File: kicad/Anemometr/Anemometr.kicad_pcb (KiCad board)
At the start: 2 copper layers, 44.9 x 45.2 mm, 161 parts, among them J10 +Z3, J11 -Z3, J12 +Z4, J13 -Z4, J14 SWD, J15 SWC, J18 1 TxD+, J19 2 TxD-, J2 Conn_01x01_Female, J20 3 RxD+, J21 4-5, J23 6 RxD-, J24 7-8, J3 RST, J36 TMP117, J37 TMP117, J38 TMP117, J39 TMP117, J4 TxD, J5 RxD, J6 +Z1, J7 -Z1, J8 +Z2, J9 -Z2, Q1 5N10, U1 TS5A3166DBVR, U10 MCP1700-3002E, U2 LMV7239, U3 TS5A3166DBVR, U4 TS5A3166DBVR, U5 STM32F103C8Tx, U6 TS5A3166DBVR, U7 LM2734Y, U8 MCP1700-5002E, U9 MCP1700-3002E, Y1 8MHz, Y2 25MHz

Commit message: изменено:      kicad/Anemometr/Anemometr-cache.lib 	изменено:      kicad/Anemometr/Anemometr.kicad_pcb 	изменено:      kicad/Anemometr/Anemometr.kicad_pcb-bak 	изменено:      kicad/Anemometr/Anemometr.sch 	изменено:      kicad/Anemometr/Anemometr.sch-bak
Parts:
- removed L6: 47uH, Inductor_SMD:L_0805_2012Metric
- C29: value 10uF -> 10nF
- C30: value 10uF -> 4.7uF
- C50: moved to B.Cu
- L4: value 47uH -> 2.2uH
- U10: value MCP1700-3002E -> AP1117-33; footprint Package_TO_SOT_SMD:SOT-23 -> Package_TO_SOT_SMD:SOT-223-3_TabPin2; moved to B.Cu
- moved C50 23.2 mm to (59.3, 88.5), turned to 0 degrees
- moved U10 13.7 mm to (57.5, 83.9), turned to 180 degrees
- moved D18 8.98 mm to (51.6, 102.9)
- moved C49 8.80 mm to (60.1, 94.5)
- moved D14 7.72 mm to (58.0, 100.7), turned to 180 degrees
- moved R43 6.84 mm to (55.0, 102.8), turned to 0 degrees
- moved L5 6.56 mm to (58.4, 102.9)
- moved R30 5.32 mm to (35.6, 87.6)
- moved R29 5.29 mm to (34.2, 87.6)
- moved D11 3.86 mm to (30.9, 85.0)
- moved R16 3.75 mm to (41.6, 86.8), turned to 0 degrees
- moved D2 3.44 mm to (26.9, 80.5), turned to 90 degrees
- moved C33 2.27 mm to (41.7, 91.4), turned to 180 degrees
- moved C47 2.11 mm to (34.7, 85.5), turned to 0 degrees
- moved C16 1.90 mm to (25.1, 81.2)
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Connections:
- C50 pad 2: Net-(C50-Pad2) -> Net-(C49-Pad1)
- U10 pad 3: Net-(C50-Pad2) -> Net-(C49-Pad1)
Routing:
- net +3.3VDAC: track 29.8 -> 40.9 mm, vias 2 -> 3
- net Net-(C49-Pad1): track 10.0 -> 20.9 mm
- net Net-(C50-Pad2): track 9.93 -> 0.00 mm
- net Net-(C22-Pad2): track 67.7 -> 63.1 mm
- net Net-(C16-Pad2): track 7.19 -> 11.8 mm
- net Net-(C45-Pad2): track 36.7 -> 32.8 mm
- net Net-(C17-Pad2): track 21.7 -> 19.0 mm
- net GND: track 236.5 -> 233.9 mm, vias 16 -> 17
- net Net-(D11-Pad2): track 14.9 -> 17.4 mm
- net Net-(C33-Pad2): track 4.31 -> 1.78 mm
- net Net-(C52-Pad1): track 7.34 -> 4.98 mm
- net Net-(D14-Pad2): track 8.81 -> 7.24 mm
- net Net-(C33-Pad1): track 4.99 -> 3.46 mm
- net +3.3VA: track 34.1 -> 33.3 mm, vias 5 -> 3
- net Net-(C34-Pad1): track 5.38 -> 6.08 mm
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
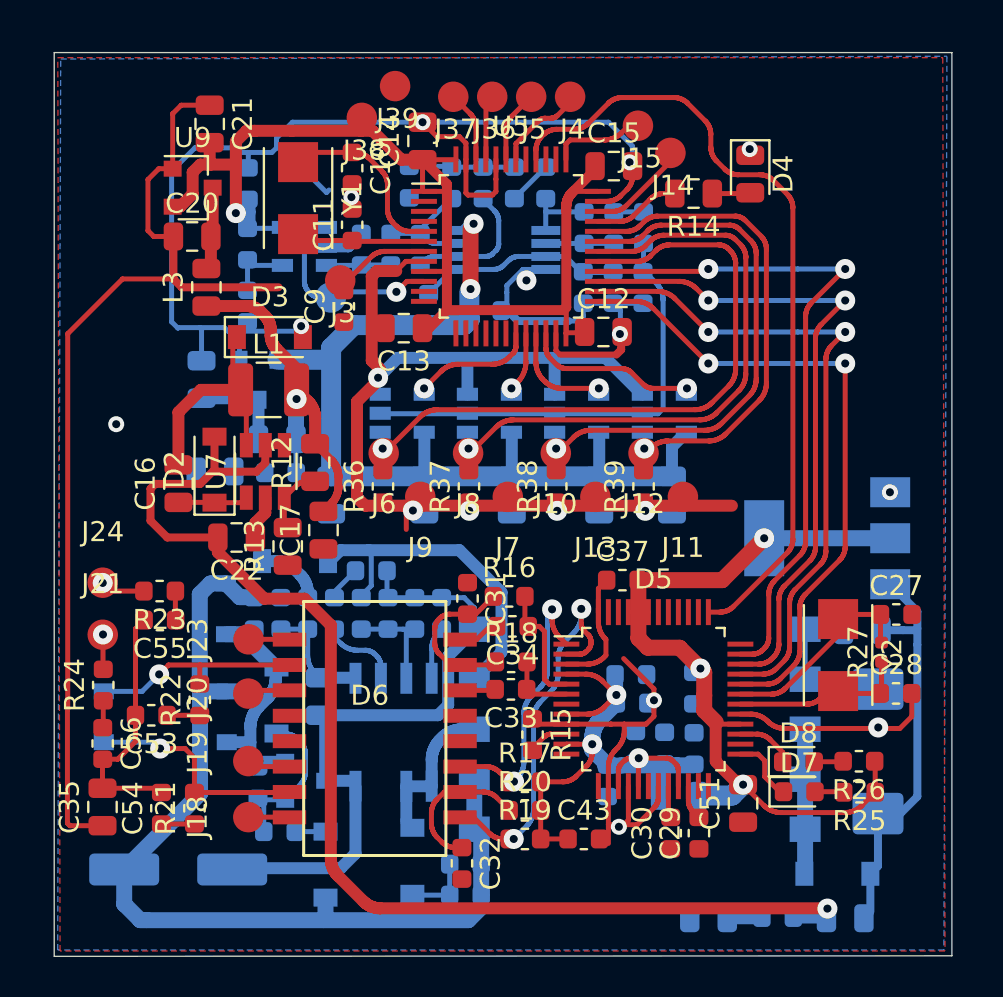
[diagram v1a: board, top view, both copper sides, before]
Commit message: изменено:      kicad/Anemometr/Anemometr.kicad_pcb 	изменено:      kicad/Anemometr/Anemometr.kicad_pcb-bak 	изменено:      kicad/Anemometr/Anemometr.sch 	изменено:      kicad/Anemometr/Anemometr.sch-bak
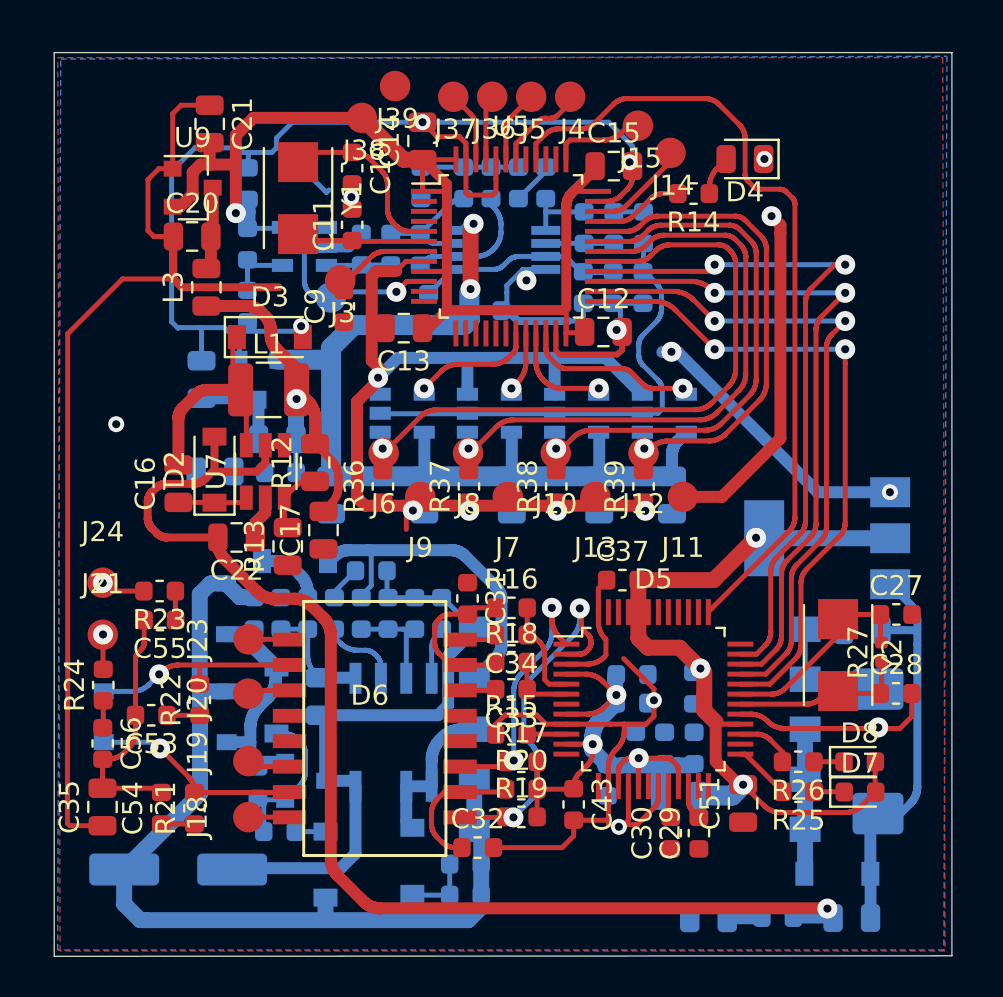
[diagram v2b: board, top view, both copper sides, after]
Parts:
- L1: value 10uH -> 22uH
- R14: footprint Resistor_SMD:R_0805_2012Metric -> Resistor_SMD:R_0603_1608Metric
- moved D8 3.06 mm to (59.1, 95.1)
- moved R25 3.05 mm to (56.1, 96.6)
- moved R26 3.04 mm to (56.1, 95.1)
- moved D7 3.04 mm to (59.2, 96.6)
- moved C43 1.80 mm to (44.8, 97.2), turned to 270 degrees
- moved R19 1.12 mm to (42.2, 97.8)
- moved C32 1.11 mm to (40.0, 99.4), turned to 0 degrees
- moved R20 1.08 mm to (42.2, 96.4)
- moved R15 1.05 mm to (41.7, 93.7), turned to 0 degrees
- moved R17 1.02 mm to (42.2, 95.1)
- moved D4 0.80 mm to (53.4, 64.9), turned to 180 degrees
- moved C3 0.60 mm to (39.3, 66.1)
- moved R9 0.59 mm to (37.2, 66.1)
- moved R16 0.58 mm to (41.7, 87.4)
- moved C34 0.43 mm to (41.7, 88.7)
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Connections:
- D7 pad 1: Net-(D5-Pad25) -> Net-(D7-Pad1)
- D7 pad 2: Net-(D7-Pad2) -> +3.3VDAC
- D8 pad 1: Net-(D5-Pad27) -> Net-(D8-Pad1)
- D8 pad 2: Net-(D8-Pad2) -> +3.3VDAC
- R25 pad 1: +3.3VDAC -> Net-(D7-Pad1)
- R25 pad 2: Net-(D7-Pad2) -> Net-(D5-Pad25)
- R26 pad 1: +3.3VDAC -> Net-(D8-Pad1)
- R26 pad 2: Net-(D8-Pad2) -> Net-(D5-Pad27)
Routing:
- net GND: track 233.9 -> 269.3 mm, vias 17 -> 19
- net Net-(D8-Pad2): track 1.46 -> 0.00 mm
- net Net-(D8-Pad1): track 0.00 -> 1.46 mm
- net Net-(D7-Pad2): track 1.45 -> 0.00 mm
- net Net-(D7-Pad1): track 0.00 -> 1.45 mm
- net Net-(D5-Pad1): track 14.0 -> 12.7 mm
- net Net-(D5-Pad2): track 18.9 -> 17.8 mm
- net +3.3VA: track 33.3 -> 32.5 mm
- net Net-(C34-Pad1): track 6.08 -> 5.26 mm
- net Net-(D6-Pad15): track 11.4 -> 10.6 mm
- net Net-(C4-Pad2): track 22.9 -> 23.7 mm
- net Net-(C45-Pad2): track 32.8 -> 32.2 mm
- net Net-(D5-Pad35): track 34.2 -> 34.8 mm
- net Net-(D5-Pad25): track 3.40 -> 2.90 mm

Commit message: изменено:      kicad/Anemometr/Anemometr.kicad_pcb 	изменено:      kicad/Anemometr/Anemometr.kicad_pcb-bak 	изменено:      kicad/Anemometr/fp-info-cache
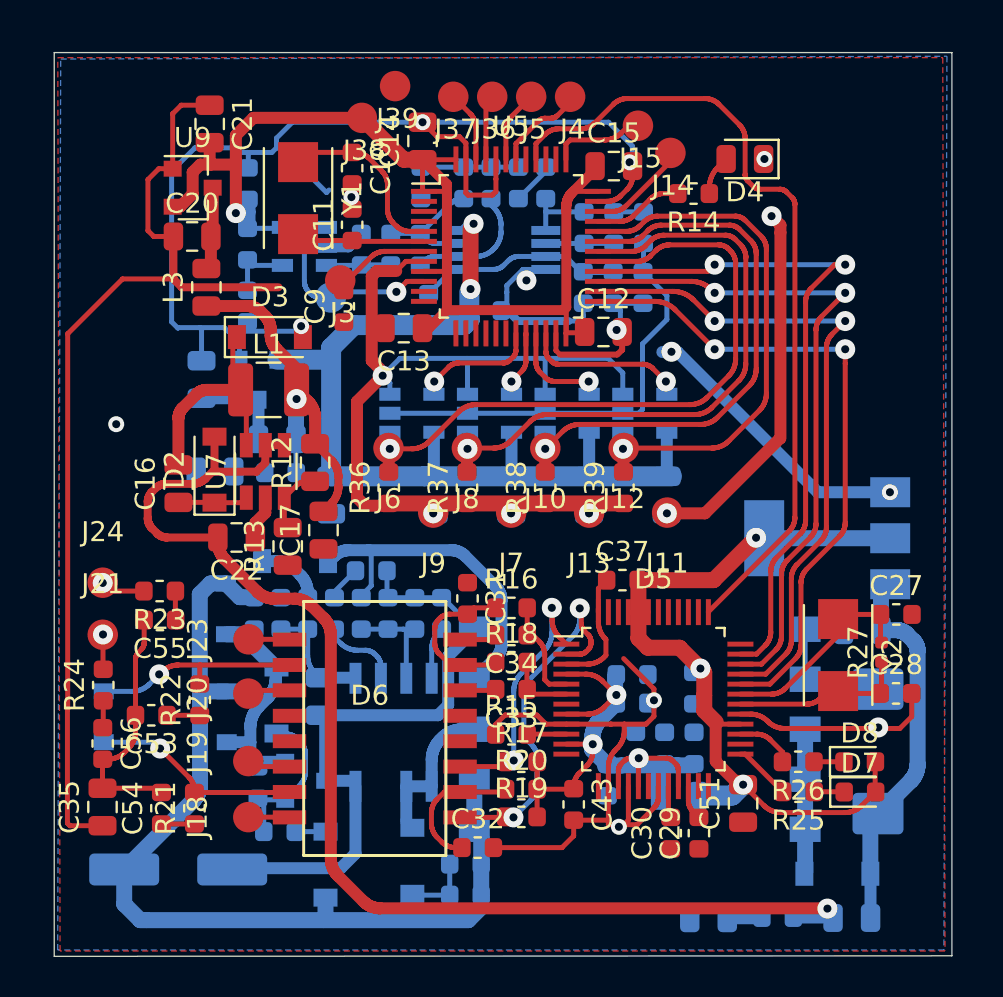
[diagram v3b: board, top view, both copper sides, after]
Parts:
- moved J11 1.11 mm to (49.5, 82.6)
- moved J12 1.02 mm to (47.3, 79.4)
- moved J9 1.02 mm to (37.8, 82.6)
- moved R39 1.01 mm to (47.3, 81.4)
- moved U6 0.98 mm to (48.4, 77.6)
- moved J13 0.85 mm to (45.6, 82.6)
- moved J7 0.81 mm to (41.7, 82.6)
- moved J10 0.58 mm to (43.4, 79.4)
- moved R38 0.55 mm to (43.4, 81.4)
- moved C26 0.51 mm to (45.6, 81.7)
- moved U1 0.48 mm to (36.8, 77.6)
- moved U4 0.47 mm to (44.5, 77.6)
- moved C24 0.47 mm to (37.8, 81.7)
- moved J6 0.35 mm to (35.6, 79.4)
- moved R36 0.30 mm to (35.6, 81.4)
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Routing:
- net GND: track 269.3 -> 267.2 mm
- net Net-(C4-Pad2): track 23.7 -> 22.0 mm
- net Net-(J12-Pad1): track 25.8 -> 27.3 mm
- net Net-(C49-Pad1): track 20.6 -> 19.1 mm
- net Net-(J6-Pad1): track 34.4 -> 33.9 mm
- net Net-(J10-Pad1): track 28.6 -> 29.1 mm

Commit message: изменено:      kicad/Anemometr/Anemometr.kicad_pcb 	изменено:      kicad/Anemometr/Anemometr.kicad_pcb-bak 	изменено:      kicad/Anemometr/Anemometr.sch 	изменено:      kicad/Anemometr/Anemometr.sch-bak
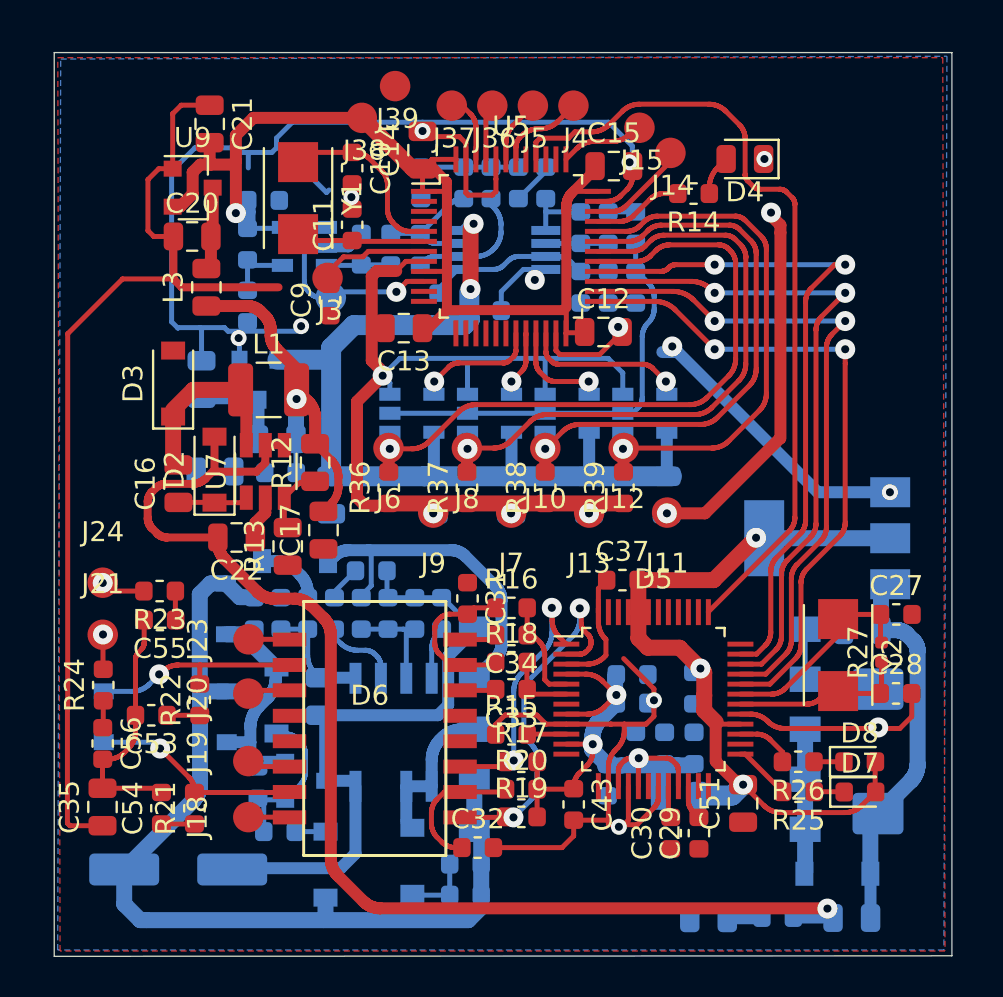
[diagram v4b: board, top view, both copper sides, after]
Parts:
- moved D3 5.37 mm to (24.8, 76.1), turned to 90 degrees
- moved C2 1.13 mm to (29.3, 67.0), turned to 0 degrees
- moved C9 0.76 mm to (32.7, 72.0)
- moved J3 0.65 mm to (32.5, 70.9)
- moved R1 0.51 mm to (38.1, 72.4)
- moved J4 0.47 mm to (44.8, 62.3)
- moved C14 0.46 mm to (37.3, 64.5)
- moved J5 0.45 mm to (42.8, 62.3)
- moved J37 0.45 mm to (38.7, 62.3)
- moved J36 0.44 mm to (40.8, 62.3)
- moved C4 0.39 mm to (47.9, 68.4)
- moved R7 0.37 mm to (47.9, 71.3)
- moved R5 0.28 mm to (46.6, 68.4)
- moved R8 0.25 mm to (46.6, 71.3)
- moved R4 0.17 mm to (45.2, 68.4)
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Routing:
- net GND: track 267.2 -> 256.7 mm
- net Net-(C16-Pad2): track 11.7 -> 9.63 mm
- net Net-(C4-Pad2): track 22.0 -> 21.4 mm
- net Net-(C8-Pad2): track 10.2 -> 9.58 mm

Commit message: изменено:      kicad/Anemometr/Anemometr-cache.lib 	изменено:      kicad/Anemometr/Anemometr.kicad_pcb 	изменено:      kicad/Anemometr/Anemometr.kicad_pcb-bak 	изменено:      kicad/Anemometr/Anemometr.sch 	изменено:      kicad/Anemometr/Anemometr.sch-bak 	изменено:      kicad/Anemometr/fp-info-cache
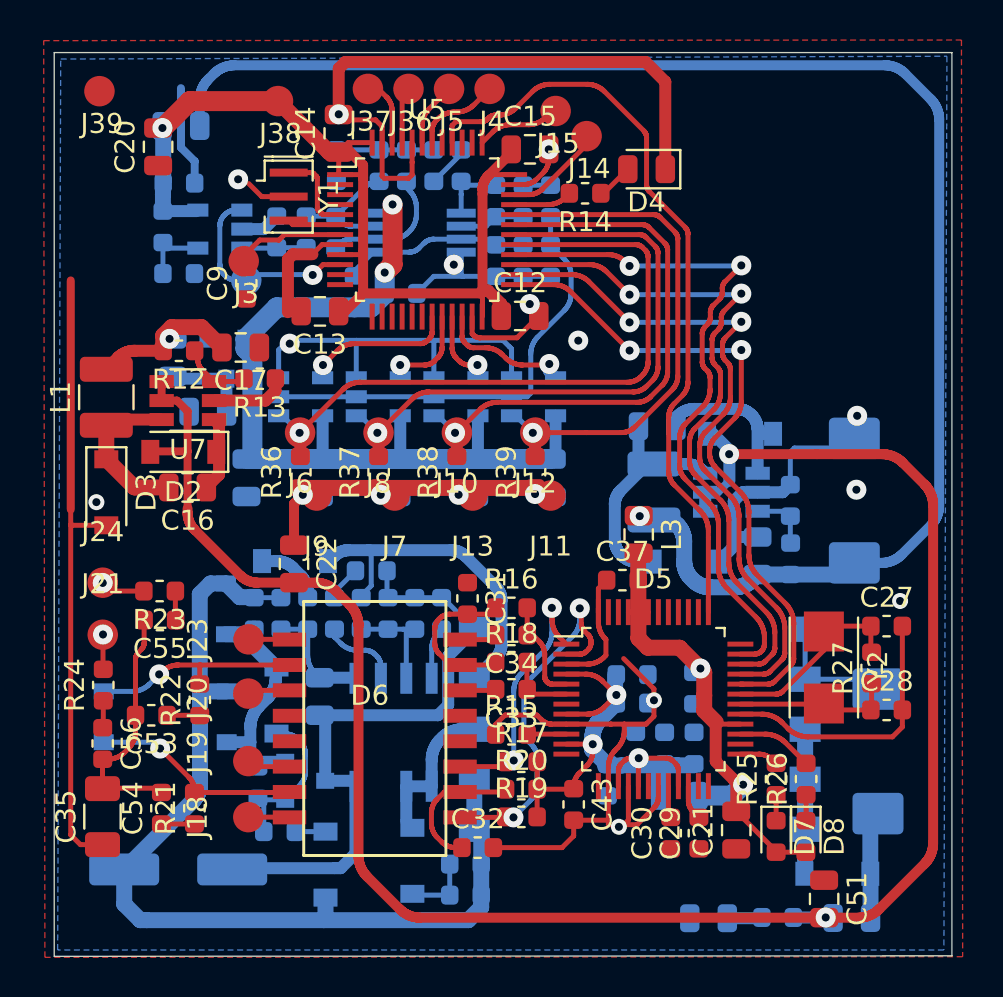
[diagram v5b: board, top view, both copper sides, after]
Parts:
- removed C10, C11: 10p, Capacitor_SMD:C_0603_1608Metric
- removed U9: MCP1700-3002E, Package_TO_SOT_SMD:SOT-23
- added C57: 22uF, Capacitor_SMD:C_0805_2012Metric, B.Cu at (54.0, 84.8)
- added C58: 1000uF, Capacitor_Tantalum_SMD:CP_EIA-7343-15_Kemet-W, B.Cu at (58.9, 82.0)
- added D20: MBR0540, Diode_SMD:D_SOD-123, B.Cu at (50.4, 85.1)
- added L6: 22uH, Inductor_SMD:L_1210_3225Metric, B.Cu at (48.9, 81.6)
- added L7: 2.2uH, Inductor_SMD:L_0805_2012Metric, B.Cu at (25.2, 63.3)
- added R35: 56k, Resistor_SMD:R_0603_1608Metric, B.Cu at (55.7, 84.9)
- C35: footprint Capacitor_SMD:C_0805_2012Metric -> Capacitor_SMD:C_1206_3216Metric
- C50: value 10uF -> 0.01uF
- D19: value LED -> MBR0540; footprint LED_SMD:LED_0805_2012Metric -> Diode_SMD:D_SOD-123
- L3: value 47uH -> 2.2uH
- R12, R13: footprint Resistor_SMD:R_0805_2012Metric -> Resistor_SMD:R_0603_1608Metric
- R27: footprint Resistor_SMD:R_0402_1005Metric -> Resistor_SMD:R_0603_1608Metric
- R44: value 2k -> 10k
- U10: value AP1117-33 -> LM2734Y; footprint Package_TO_SOT_SMD:SOT-223-3_TabPin2 -> Package_TO_SOT_SMD:TSOT-23-6
- Y1: footprint Crystal:Crystal_SMD_Qantek_QC5CB-2Pin_5x3.2mm -> Crystal:Resonator_SMD_muRata_CSTxExxV-3Pin_3.0x1.1mm
- moved C21 44.0 mm to (53.0, 98.5), turned to 90 degrees
- moved D19 26.3 mm to (53.2, 78.7), turned to 180 degrees
- moved R44 25.5 mm to (55.7, 82.0), turned to 270 degrees
- moved L3 24.9 mm to (48.1, 83.7), turned to 270 degrees
- moved J39 14.8 mm to (21.1, 61.5)
- moved C50 14.5 mm to (49.0, 78.3), turned to 180 degrees
- moved C17 10.0 mm to (28.2, 74.3), turned to 180 degrees
- moved R12 8.81 mm to (25.1, 74.5), turned to 180 degrees
- moved R13 8.50 mm to (29.1, 75.9), turned to 180 degrees
- moved L1 8.12 mm to (21.5, 76.8), turned to 90 degrees
- moved L2 6.63 mm to (24.8, 74.9), turned to 270 degrees
- moved D3 6.38 mm to (21.5, 81.6), turned to 270 degrees
- moved C51 6.26 mm to (57.4, 101.9), turned to 270 degrees
- moved J13 5.89 mm to (39.8, 81.7)
- moved J9 5.89 mm to (32.0, 81.7)
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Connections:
- C20 pad 2: Net-(C20-Pad2) -> +3V3
- C21 pad 2: +3V3 -> +3.3VDAC
- C50 pad 1: GND -> Net-(C50-Pad1)
- C50 pad 2: Net-(C49-Pad1) -> Net-(C50-Pad2)
- C51 pad 2: +3.3VDAC -> Net-(C22-Pad2)
- D19 pad 1: GND -> Net-(C50-Pad1)
- D19 pad 2: Net-(D19-Pad2) -> Net-(C22-Pad2)
- L3 pad 1: Net-(C17-Pad2) -> Net-(C57-Pad2)
- L3 pad 2: Net-(C20-Pad2) -> +3.3VDAC
- R44 pad 1: Net-(C17-Pad2) -> GND
- R44 pad 2: Net-(D19-Pad2) -> Net-(R35-Pad1)
- U10 pad 1: GND -> Net-(C50-Pad1)
- U10 pad 2: +3.3VDAC -> GND
- U10 pad 3: Net-(C49-Pad1) -> Net-(R35-Pad1)
- U5 pad 6: Net-(C11-Pad1) -> Net-(U5-Pad6)
- Y1 pad 2: Net-(C11-Pad1) -> GND
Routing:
- net Net-(C57-Pad2): track 0.00 -> 78.4 mm, vias 0 -> 1
- net GND: track 256.7 -> 200.1 mm, vias 19 -> 17
- net Net-(C22-Pad2): track 62.8 -> 99.8 mm, vias 1 -> 2
- net +3.3VDAC: track 40.5 -> 25.8 mm, vias 3 -> 2
- net Net-(C49-Pad1): track 19.1 -> 5.38 mm
- net Net-(C50-Pad2): track 0.00 -> 11.3 mm
- net Net-(C17-Pad2): track 19.0 -> 7.72 mm
- net Net-(C50-Pad1): track 0.00 -> 8.20 mm
- net +3V3: track 56.6 -> 49.3 mm
- net Net-(C11-Pad1): track 6.44 -> 0.00 mm
- net Net-(U5-Pad5): track 10.5 -> 4.34 mm
- net Net-(C20-Pad2): track 4.17 -> 0.00 mm
- net Net-(R35-Pad1): track 0.00 -> 3.09 mm
- net +5VA: track 47.5 -> 44.5 mm
- net Net-(U5-Pad6): track 0.00 -> 2.65 mm
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
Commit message: изменено:      kicad/Anemometr/Anemometr.kicad_pcb 	изменено:      kicad/Anemometr/Anemometr.kicad_pcb-bak 	изменено:      kicad/Anemometr/Anemometr.sch 	изменено:      kicad/Anemometr/Anemometr.sch-bak 	изменено:      stm32cubeide/Anemometer/Core/Inc/main.h 	изменено:      stm32cubeide/Anemometer/Core/Inc/wizchip_conf.h 	изменено:      stm32cubeide/Anemometer/Core/Src/dhcp.c 	изменено:      stm32cubeide/Anemometer/Core/Src/main.c 	изменено:      stm32cubeide/Anemometer/Release/Anemometer.bin 	изменено:      stm32cubeide/Anemometer/Release/Anemometer.elf 	изменено:      stm32cubeide/Anemometer/Release/Anemometer.list 	изменено:      stm32cubeide/Anemometer/Release/Anemometer.map 	изменено:      stm32cubeide/Anemometer/Release/Core/Src/main.o 	изменено:      stm32cubeide/Anemometer/Release/Core/Src/main.su 	изменено:      stm32cubeide/Anemometer/Release/Core/Src/stm32f1xx_it.o
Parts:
- moved C53 4.52 mm to (24.9, 88.4)
- moved R21 2.55 mm to (24.9, 95.0), turned to 180 degrees
- moved R22 2.55 mm to (24.9, 89.7), turned to 180 degrees
- moved C35 1.27 mm to (21.8, 99.0)
- moved C55 1.26 mm to (24.9, 87.0)
- moved C54 1.22 mm to (24.9, 96.4), turned to 180 degrees
- moved R23 1.20 mm to (24.9, 85.6)
- moved C9 0.97 mm to (28.3, 70.2)
- moved J3 0.86 mm to (28.3, 69.2)
- moved D3 0.49 mm to (21.8, 81.2)
- moved L1 0.45 mm to (21.8, 76.6)
- moved R44 0.23 mm to (55.7, 81.8)
- moved D2 0.11 mm to (25.4, 79.6)
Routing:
- net GND: track 200.1 -> 195.2 mm
- net Net-(D6-Pad15): track 10.6 -> 14.5 mm
- net Net-(C35-Pad2): track 12.6 -> 15.0 mm
- net Net-(D6-Pad10): track 10.7 -> 11.7 mm
- net Net-(D10-Pad2): track 2.23 -> 3.04 mm
